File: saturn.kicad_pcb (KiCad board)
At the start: 4 copper layers, 100 x 66 mm, 103 parts, among them J1 Conn_01x04_Pin, J10 Conn_01x04, J11 USB_B_Micro, J12 USB_C_Receptacle_USB2.0, J13 Conn_01x03, J14 Conn_01x04_Pin, J2 PMOD0_FULL, J3 Conn_01x06, J4 Conn_01x06, J6 Conn_01x10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

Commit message: Release v1.0.0
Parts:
- added R19: 10k, Resistor_SMD:R_0402_1005Metric, F.Cu at (96.8, 60.9)
- J13: value Conn_01x03 -> S3B-XH-A-1(LF)(SN)
- U9: value WS2812B -> XL-2020RGBC-WS2812B
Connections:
- RN6 pad 1: (no net) -> unconnected-(RN6A-R1.1-Pad1)
- RN6 pad 8: (no net) -> unconnected-(RN6A-R1.2-Pad8)
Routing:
- net +3V3: track 236.7 -> 253.9 mm, vias 17 -> 18
- net /SMART_LEDS: track 64.0 -> 75.7 mm
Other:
- board text added: "2026"
- board text added: "Power from one source only"
- board text added: "Saturn v1.0.0"
- board text removed: "LED Strip"
- board text removed: "Power from single source only"
- board text removed: "Saturn v1"

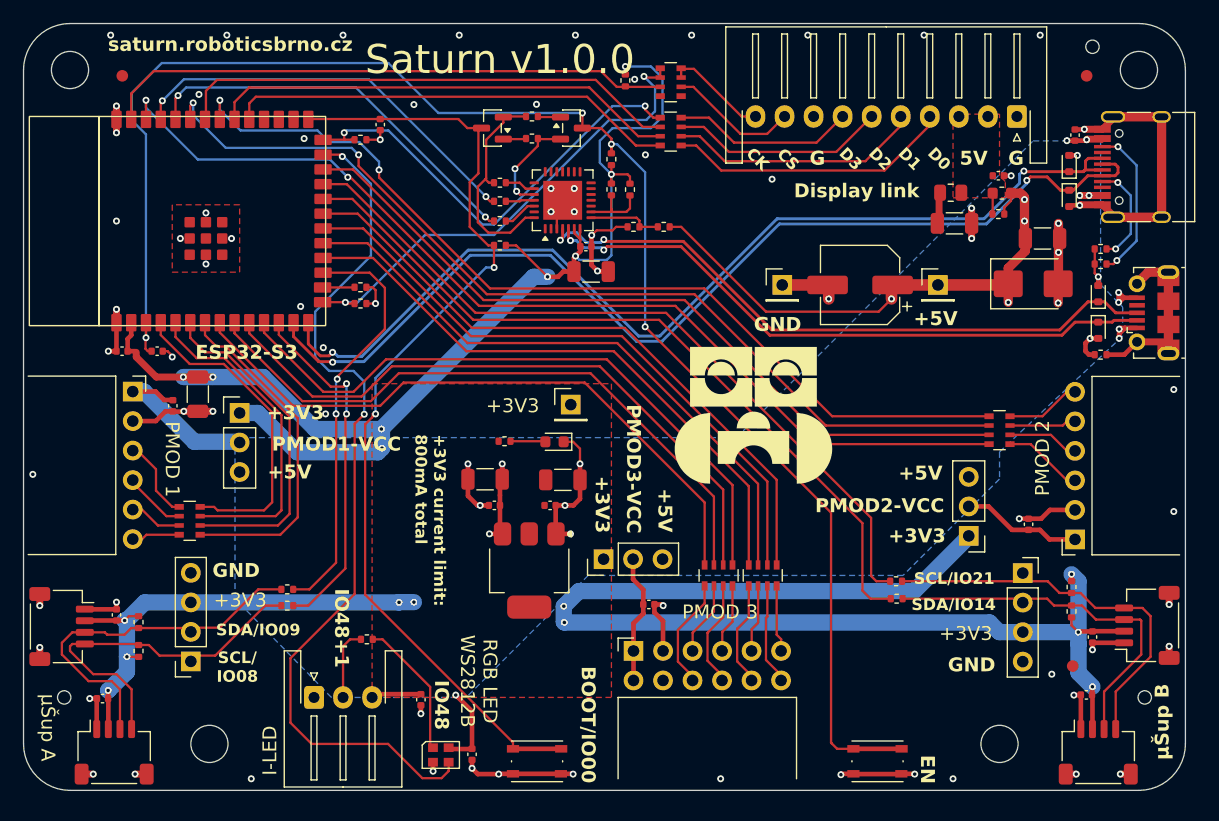
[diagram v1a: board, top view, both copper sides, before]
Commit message: Fix PMOD ADC pin assignment, tune silkscreen
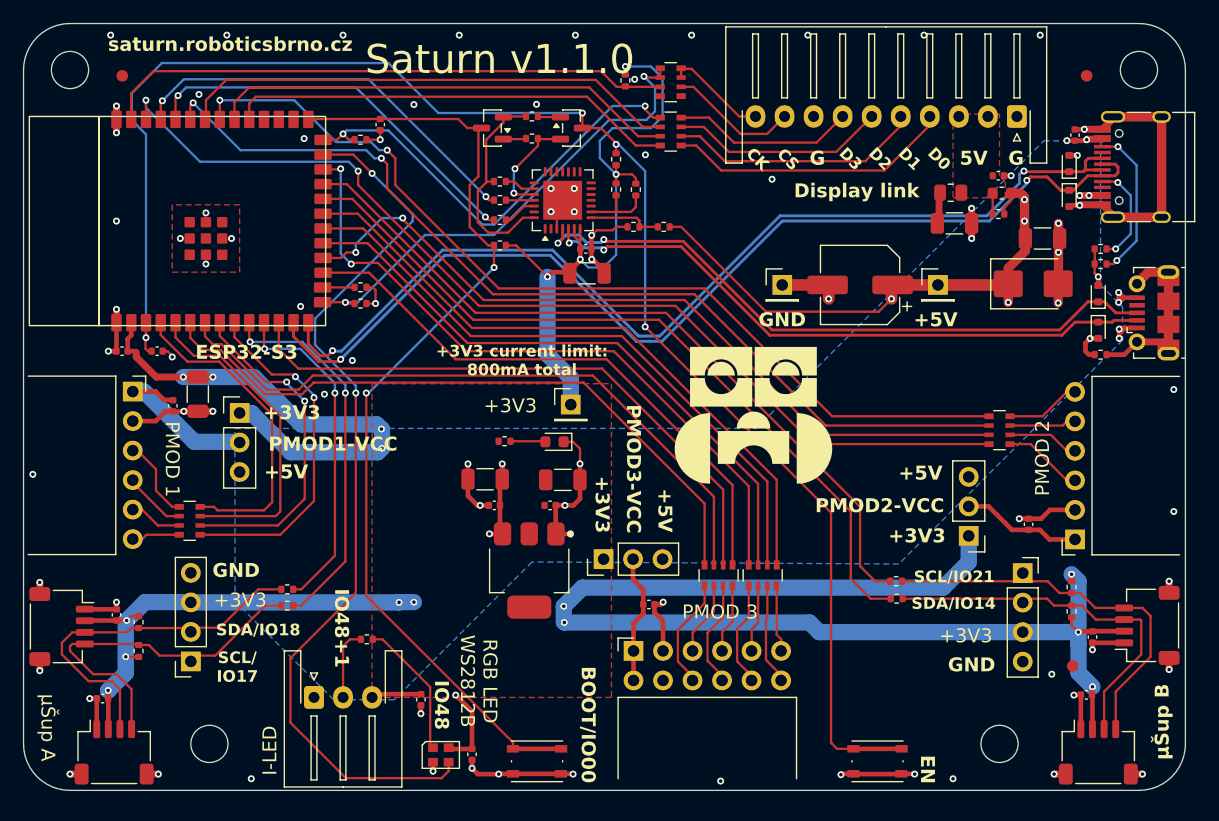
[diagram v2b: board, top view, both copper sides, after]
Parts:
- removed H5, H6, H7: MountingHole, MountingHole:ToolingHole_1.152mm
- J2: value PMOD0_FULL -> PMOD3_FULL
- moved R13 0.51 mm to (97.7, 70.3)
- moved R10 0.41 mm to (96.0, 70.3)
- moved R2 0.41 mm to (96.0, 67.7)
- moved C24 0.38 mm to (93.5, 77.5)
- moved C14 0.20 mm to (93.4, 75.4)
- moved R34 0.10 mm to (86.0, 69.6)
- moved R17 0.10 mm to (86.0, 72.9)
- moved R18 0.10 mm to (86.0, 71.2)
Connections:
- net /PMOD0_IO1 renamed /PMOD3_IO1
- net /PMOD0_IO2 renamed /PMOD3_IO2
- net /PMOD0_IO7 renamed /PMOD3_IO7
- RN3 pad 8: /PMOD0_IO8 -> /PMOD3_IO8
- RN4 pad 5: /PMOD0_IO3 -> /PMOD3_IO3
- RN4 pad 6: /PMOD0_IO9 -> /PMOD3_IO9
- RN4 pad 7: /PMOD0_IO4 -> /PMOD3_IO4
- RN4 pad 8: /PMOD0_IO10 -> /PMOD3_IO10
- U1 pad 10: /PMOD0_IO9 -> /I2CA_SCL
- U1 pad 11: /PMOD0_IO3 -> /I2CA_SDA
- U1 pad 12: /I2CA_SCL -> /PMOD3_IO9
- U1 pad 17: /I2CA_SDA -> /PMOD3_IO3
- U1 pad 18: /PMOD0_IO8 -> /PMOD2_IO3
- U1 pad 24: /PMOD2_IO3 -> /PMOD3_IO8
- U1 pad 6: /PMOD1_IO2 -> /PMOD3_IO10
- U1 pad 7: /PMOD1_IO1 -> /PMOD3_IO4
- U1 pad 8: /PMOD0_IO10 -> /PMOD1_IO2
- U1 pad 9: /PMOD0_IO4 -> /PMOD1_IO1
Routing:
- net /PMOD3_IO8: track 0.00 -> 59.1 mm, vias 0 -> 2
- net /PMOD3_IO10: track 0.00 -> 57.6 mm
- net /PMOD3_IO4: track 0.00 -> 57.6 mm
- net /PMOD0_IO9: track 55.9 -> 0.00 mm
- net /PMOD0_IO4: track 55.9 -> 0.00 mm
- net /PMOD0_IO3: track 55.8 -> 0.00 mm
- net /PMOD0_IO10: track 55.7 -> 0.00 mm
- net /PMOD3_IO9: track 0.00 -> 52.0 mm
- net /PMOD0_IO8: track 51.6 -> 0.00 mm
- net /PMOD3_IO3: track 0.00 -> 49.7 mm
- net /I2CA_SDA: track 35.9 -> 29.2 mm
- net +3V3: track 253.9 -> 247.8 mm
- net /I2CA_SCL: track 30.6 -> 32.7 mm
- net /SMART_LEDS: track 75.7 -> 77.5 mm
- net GND: track 147.7 -> 146.6 mm
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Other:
- board text added: "IO04 IO05 IO15 IO16"
- board text added: "IO06 IO08 IO47 IO12"
- board text added: "IO07 IO09 IO11 IO13"
- board text added: "IO40 IO42 IO10 IO02"
- board text added: "SCL/ IO17"
- board text added: "SCL/IO17"
- board text added: "SDA/IO18"
- board text added: "Saturn v1.1.0"
- board text removed: "IO04 IO05 IO06 IO07"
- board text removed: "IO15 IO17 IO10 IO12"
- board text removed: "IO16 IO18 IO11 IO13"
- board text removed: "IO40 IO42 IO47 IO02"
- board text removed: "SCL/ IO08"
- board text removed: "SDA/IO09"
- board text removed: "Saturn v1.0.0"

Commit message: Add PMOD polarity mark on Top
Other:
- board text added: "+"
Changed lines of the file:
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@@
+		)
+	)
+	(gr_text "+"
+		(at 56.7 87.45 0)
+		(layer "F.SilkS")
+		(effects
+			(font
+				(size 1.2 1.2)
+				(thickness 0.25)
+				(bold yes)
+			)
 		)
 	)
@@
 		)
 	)
+	(gr_text "+"
+		(at 97.5 107.4 0)
+		(layer "F.SilkS")
+		(effects
+			(font
+				(size 1.2 1.2)
+				(thickness 0.25)
+				(bold yes)
+			)
+		)
+	)
 	(gr_text "GND"
 		(at 110.3 81.5 0)
@@
 		)
 	)
+	(gr_text "+"
+		(at 133.25 100.3 0)
+		(layer "F.SilkS")
+		(effects
+			(font
+				(size 1.2 1.2)
+				(thickness 0.25)
+				(bold yes)
+			)
+		)
+	)
 	(gr_text "+5V"
 		(at 67.6 95.3 0)
@@
 		)
 	)
-	(gr_text "I-LED"
-		(at 66.2 118.575 90)
-		(layer "F.SilkS")
-		(effects
-			(font
-				(size 1.2 1.2)
-				(thickness 0.25)
-			)
-		)
-	)
 	(gr_text "PMOD 2"
 		(at 132.7 93.4 90)
@@
 		(layer "F.SilkS")
 		(effects
+			(font
+				(size 1.2 1.2)
+				(thickness 0.25)
+			)
+		)
+	)
+	(gr_text "I-LED"
+		(at 66.2 118.575 270)
+		(layer "F.SilkS")
+		(effects

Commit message: Fix 5V unroute
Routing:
- net +5V: track 73.9 -> 77.6 mm
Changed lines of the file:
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@@
 	)
 	(gr_text "+"
+		(at 75 111.6 0)
+		(layer "F.SilkS")
+		(effects
+			(font
+				(size 1.2 1.2)
+				(thickness 0.25)
+				(bold yes)
+			)
+		)
+	)
+	(gr_text "+"
 		(at 97.5 107.4 0)
 		(layer "F.SilkS")
@@
 	)
 	(segment
+		(start 83.6 118.42)
+		(end 83.6 115.55)
+		(width 0.4)
+		(layer "F.Cu")
+		(net "+5V")
+	)
+	(segment
 		(start 131.225 75.575)
 		(end 131.225 74.7)
@@
 	)
 	(segment
-		(start 82.199293 113.797765)
-		(end 83.6 115.198472)
-		(width 0.4)
-		(layer "F.Cu")
-		(net "+5V")
-	)
-	(segment
 		(start 137.855 65.9)
 		(end 137.805 65.95)
@@
 	)
 	(segment
-		(start 83.6 115.198472)
-		(end 83.6 118.42)
-		(width 0.4)
-		(layer "F.Cu")
-		(net "+5V")
-	)
-	(segment
 		(start 130.80104 70.6)
 		(end 129.9875 70.6)
@@
 	)
 	(segment
+		(start 83.6 115.55)
+		(end 79.35 111.3)
+		(width 0.4)
+		(layer "F.Cu")
+		(net "+5V")
+	)
+	(segment
 		(start 139.8 82.2)
 		(end 139.3 82.7)
@@
 	)
 	(via
-		(at 82.199293 113.797765)
+		(at 79.35 111.3)
 		(size 0.6)
 		(drill 0.3)
@@
 	)
 	(segment
+		(start 77.32 105.82)
+		(end 59.4 105.82)
+		(width 1.4)
+		(layer "B.Cu")
+		(net "+3V3")
+	)
+	(segment
 		(start 96.8 59.7)
 		(end 99 59.7)
@@
 	)
 	(segment
-		(start 77.28 105.82)
-		(end 59.4 105.82)
-		(width 1.4)
-		(layer "B.Cu")
-		(net "+3V3")
-	)
-	(segment
 		(start 91.5 107.5)
 		(end 91.55 107.55)
@@
 		(layer "F.Cu")
 		(hatch none 0.1)
-		(priority 30012)
+		(priority 30011)
 		(attr
 			(teardrop
@@
 		(layer "F.Cu")
 		(hatch none 0.1)
-		(priority 30007)
+		(priority 30009)
 		(attr
 			(teardrop
@@
 		(layer "F.Cu")
 		(hatch none 0.1)
-		(priority 30010)
+		(priority 30012)
 		(attr
 			(teardrop
@@
 		(layer "F.Cu")
 		(hatch none 0.1)
-		(priority 30011)
+		(priority 30010)
 		(attr
 			(teardrop
@@
 		(layer "F.Cu")
 		(hatch none 0.1)
-		(priority 30005)
+		(priority 30003)
 		(attr
 			(teardrop
@@
 		(layer "F.Cu")
 		(hatch none 0.1)
-		(priority 30003)
+		(priority 30004)
 		(attr
 			(teardrop
@@
 		(layer "F.Cu")
 		(hatch none 0.1)
-		(priority 30004)
+		(priority 30005)
 		(attr
 			(teardrop
@@
 		(layer "F.Cu")
 		(hatch none 0.1)
-		(priority 30009)
+		(priority 30008)
 		(attr
 			(teardrop
@@
 		(layer "F.Cu")
 		(hatch none 0.1)
-		(priority 30008)
+		(priority 30007)
 		(attr
 			(teardrop
@@
 		(layer "B.Cu")
 		(hatch none 0.1)
-		(priority 30001)
+		(priority 30004)
 		(attr
 			(teardrop
@@
 		(layer "B.Cu")
 		(hatch none 0.1)
-		(priority 30004)
+		(priority 30003)
 		(attr
 			(teardrop
@@
 		(layer "B.Cu")
 		(hatch none 0.1)
-		(priority 30003)
+		(priority 30001)
 		(attr
 			(teardrop

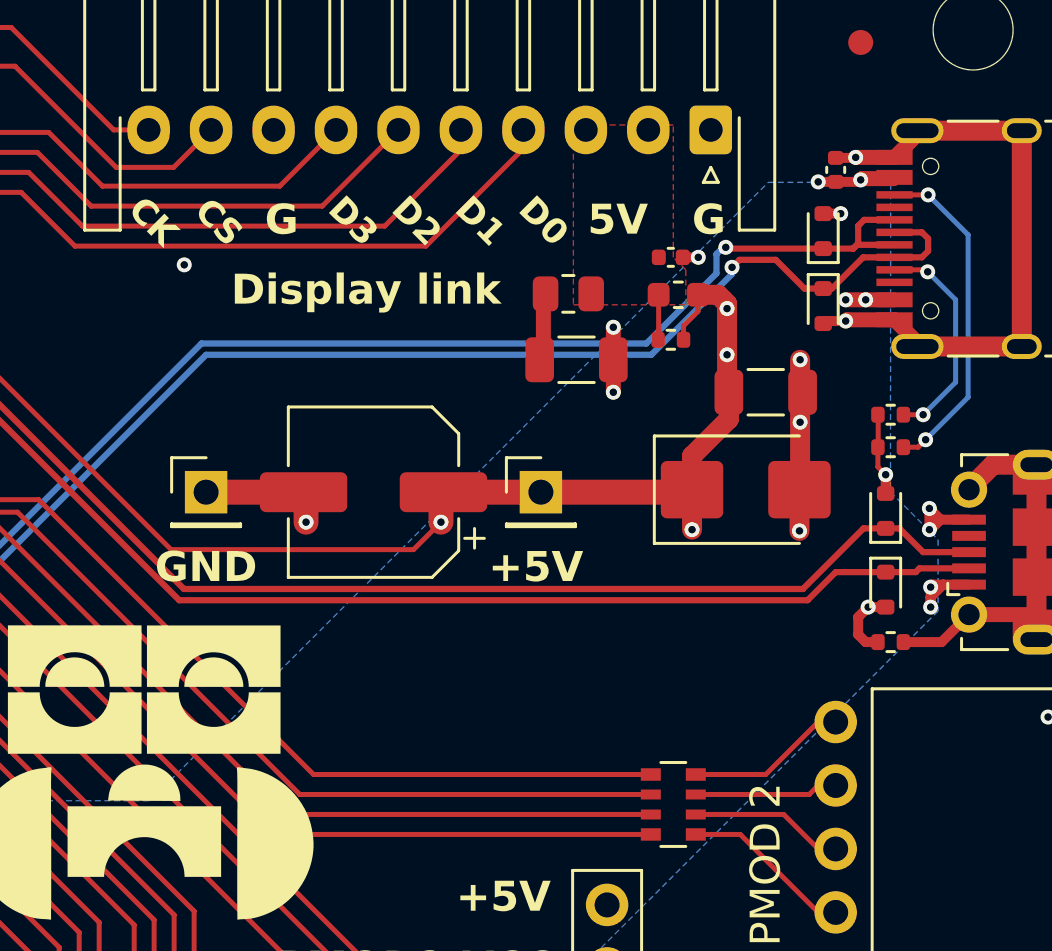
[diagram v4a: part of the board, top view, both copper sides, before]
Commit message: Use unipolar TVS diodes, tune switch values
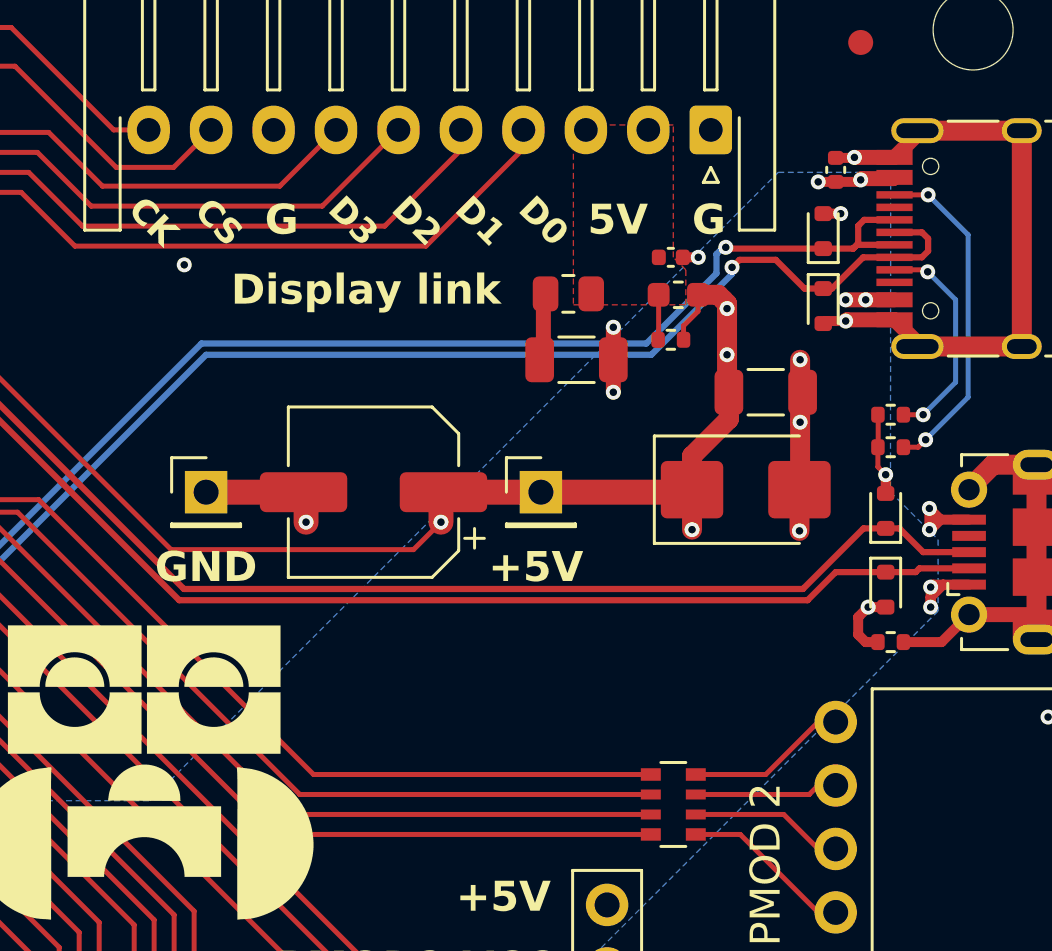
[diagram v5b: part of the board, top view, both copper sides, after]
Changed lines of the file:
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@@
 	)
 	(segment
+		(start 136.25 65.1)
+		(end 137.855 65.1)
+		(width 0.6)
+		(layer "F.Cu")
+		(net "GND")
+	)
+	(segment
 		(start 136 116.725)
 		(end 136 113.78)
@@
 	)
 	(segment
-		(start 137.855 65.1)
-		(end 136.3 65.1)
-		(width 0.6)
-		(layer "F.Cu")
-		(net "GND")
-	)
-	(segment
 		(start 57.4 84.2)
 		(end 57.8 84.6)
@@
 	)
 	(segment
-		(start 136.28 65.12)
-		(end 135.5 65.12)
-		(width 0.4)
-		(layer "F.Cu")
-		(net "GND")
-	)
-	(segment
 		(start 138.77 72.67)
 		(end 138.77 72.515)
@@
 	)
 	(segment
+		(start 135.5 65.12)
+		(end 136.23 65.12)
+		(width 0.4)
+		(layer "F.Cu")
+		(net "GND")
+	)
+	(segment
 		(start 137.5 83.1)
 		(end 136.8 83.1)
@@
 	)
 	(segment
+		(start 136.23 65.12)
+		(end 136.25 65.1)
+		(width 0.4)
+		(layer "F.Cu")
+		(net "GND")
+	)
+	(segment
 		(start 135.1 71.65)
 		(end 135 71.75)
@@
 	)
 	(segment
-		(start 136.3 65.1)
-		(end 136.28 65.12)
-		(width 0.4)
-		(layer "F.Cu")
-		(net "GND")
-	)
-	(segment
 		(start 120.55 120.575)
 		(end 121.675 120.575)
@@
 	)
 	(via
-		(at 136.3 65.1)
+		(at 136.25 65.1)
 		(size 0.6)
 		(drill 0.3)
@@
 			(pts
 				(xy 139.6 80.4) (xy 139.599628 83.255144) (xy 120.335025 102.514721) (xy 88.76991 102.342169) (xy 76.9 114.2)
-				(xy 71.695294 114.2) (xy 63.204963 105.720174) (xy 63.195757 90.85) (xy 108.05 90.85) (xy 132.8 66.1)
-				(xy 137.65 66.1) (xy 137.7 66.15) (xy 137.692924 78.490736)
+				(xy 71.695294 114.2) (xy 63.204963 105.720174) (xy 63.195757 90.85) (xy 108.05 90.85) (xy 133.2 65.7)
+				(xy 137.25 65.7) (xy 137.7 66.15) (xy 137.692924 78.490736)
 			)
 		)

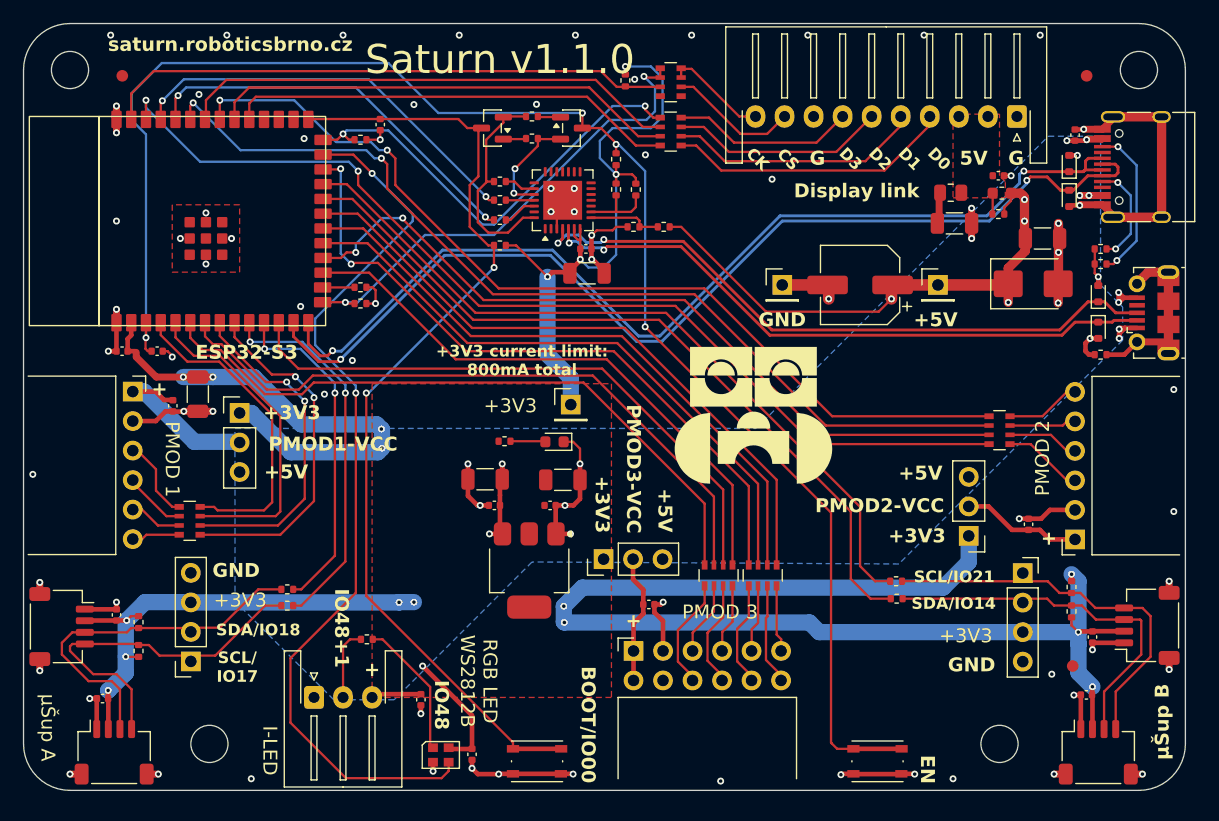
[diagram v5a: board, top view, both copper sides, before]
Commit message: Use SMT PMOD jumper header
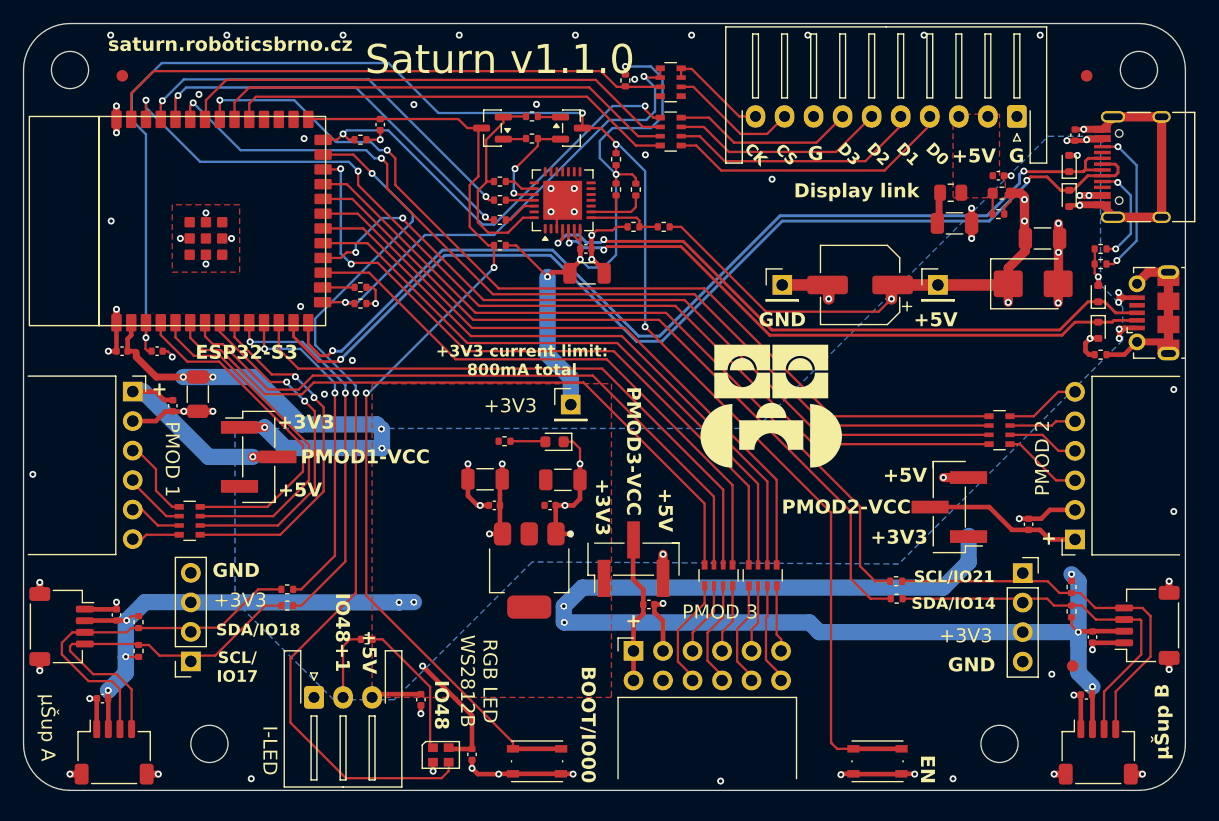
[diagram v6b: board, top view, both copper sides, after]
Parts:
- D6, D7, D8, D9: value H3V3LD5B -> PESD3V3L1UB
- JP1, JP2, JP3: footprint Connector_PinHeader_2.54mm:PinHeader_1x03_P2.54mm_Vertical -> PinHeader_jumper:PinHeader_1x03_P2.54mm_Vertical_SMD_Pin1Left_LargePads
- SW2: value EN -> SKRPABE010
- SW3: value BOOT -> SKRPABE010
- moved JP2 4.12 mm to (65.2, 93.3)
- moved JP3 2.99 mm to (124.7, 97.6)
- moved JP1 2.58 mm to (97.5, 102.1)
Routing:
- net +5V: track 77.6 -> 81.8 mm, vias 13 -> 15
- net Net-(J3-Pin_6): track 14.8 -> 18.6 mm, vias 0 -> 1
- net Net-(J4-Pin_6): track 10.3 -> 13.6 mm
- net /PMOD1_IO4: track 27.6 -> 29.6 mm
- net /PMOD1_IO3: track 28.4 -> 30.3 mm
- net Net-(J2-Pin_12): track 11.2 -> 12.9 mm
- net +3V3: track 247.8 -> 247.0 mm, vias 18 -> 19
- net /PMOD1_IO1: track 30.3 -> 30.9 mm
- net /PMOD1_IO2: track 29.2 -> 29.7 mm
